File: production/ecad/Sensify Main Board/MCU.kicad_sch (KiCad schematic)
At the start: 0 parts

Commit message: step, mod, sym files for ESP32-WROOM-32, imported into schematic
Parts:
- added U1: ESP32-WROOM-32, ESP32-WROOM-32:MODULE_ESP32-WROOM-32, symbol ESP32-WROOM-32:ESP32-WROOM-32
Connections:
- new net: U1.1 (GND), U1.15 (GND), U1.38 (GND), U1.39_1 (GND), U1.39_10 (GND), U1.39_11 (GND), U1.39_12 (GND), U1.39_13 (GND), U1.39_14 (GND), U1.39_15 (GND), U1.39_16 (GND), U1.39_17 (GND), U1.39_18 (GND), U1.39_19 (GND), U1.39_2 (GND), U1.39_20 (GND), U1.39_21 (GND), U1.39_3 (GND), U1.39_4 (GND), U1.39_5 (GND), U1.39_6 (GND), U1.39_7 (GND), U1.39_8 (GND), U1.39_9 (GND)
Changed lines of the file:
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@@
 (kicad_sch (version 20230121) (generator eeschema)
   (paper "A4")
+  (symbol (lib_id "ESP32-WROOM-32:ESP32-WROOM-32") (at 151.13 100.33 0) (unit 1)
+    (in_bom yes) (on_board yes) (dnp no) (fields_autoplaced)
+    (property "Reference" "U1" (at 151.13 59.69 0)
+      (effects (font (size 1.27 1.27)))
+    )
+    (property "Value" "ESP32-WROOM-32" (at 151.13 62.23 0)
+      (effects (font (size 1.27 1.27)))
+    )
+    (property "Footprint" "ESP32-WROOM-32:MODULE_ESP32-WROOM-32" (at 151.13 100.33 0)
+      (effects (font (size 1.27 1.27)) (justify bottom) hide)
+    )
+    (property "Datasheet" "" (at 151.13 100.33 0)
+      (effects (font (size 1.27 1.27)) hide)
+    )
+    (property "MF" "Espressif Systems" (at 151.13 100.33 0)
+      (effects (font (size 1.27 1.27)) (justify bottom) hide)
+    )
+    (property "MAXIMUM_PACKAGE_HEIGHT" "3.2 mm" (at 151.13 100.33 0)
+      (effects (font (size 1.27 1.27)) (justify bottom) hide)
+    )
+    (property "Package" "None" (at 151.13 100.33 0)
+      (effects (font (size 1.27 1.27)) (justify bottom) hide)
+    )
+    (property "Price" "None" (at 151.13 100.33 0)
+      (effects (font (size 1.27 1.27)) (justify bottom) hide)
+    )
+    (property "Check_prices" "https://www.snapeda.com/parts/ESP32-WROOM-32/Espressif+Systems/view-part/?ref=eda" (at 151.13 100.33 0)
+      (effects (font (size 1.27 1.27)) (justify bottom) hide)
+    )
+    (property "STANDARD" "Manufacturer Recommendations" (at 151.13 100.33 0)
+      (effects (font (size 1.27 1.27)) (justify bottom) hide)
+    )
+    (property "PARTREV" "2.9" (at 151.13 100.33 0)
+      (effects (font (size 1.27 1.27)) (justify bottom) hide)
+    )
+    (property "SnapEDA_Link" "https://www.snapeda.com/parts/ESP32-WROOM-32/Espressif+Systems/view-part/?ref=snap" (at 151.13 100.33 0)
+      (effects (font (size 1.27 1.27)) (justify bottom) hide)
+    )
+    (property "MP" "ESP32-WROOM-32" (at 151.13 100.33 0)
+      (effects (font (size 1.27 1.27)) (justify bottom) hide)
+    )
+    (property "Description" "\nBluetooth, WiFi 802.11b/g/n, Bluetooth v4.2 +EDR, Class 1, 2 and 3 Transceiver Module 2.4GHz ~ 2.5GHz Antenna Not Included, U.FL Surface Mount\n" (at 151.13 100.33 0)
+      (effects (font (size 1.27 1.27)) (justify bottom) hide)
+    )
+    (property "Availability" "In Stock" (at 151.13 100.33 0)
+      (effects (font (size 1.27 1.27)) (justify bottom) hide)
+    )
+    (property "MANUFACTURER" "Espressif Systems" (at 151.13 100.33 0)
+      (effects (font (size 1.27 1.27)) (justify bottom) hide)
+    )
+    (pin "39_6")
+    (pin "6")
+    (pin "3")
+    (pin "39_5")
+    (pin "4")
+    (pin "39_13")
+    (pin "9")
+    (pin "25")
+    (pin "39_3")
+    (pin "34")
+    (pin "38")
+    (pin "24")
+    (pin "8")
+    (pin "22")
+    (pin "32")
+    (pin "39_11")
+    (pin "37")
+    (pin "39_15")
+    (pin "39_12")
+    (pin "21")
+    (pin "39_16")
+    (pin "27")
+    (pin "39_18")
+    (pin "39_19")
+    (pin "29")
+    (pin "33")
+    (pin "20")
+    (pin "39_14")
+    (pin "39_21")
+    (pin "39_4")
+    (pin "39_9")
+    (pin "39_10")
+    (pin "7")
+    (pin "5")
+    (pin "36")
+    (pin "39_2")
+    (pin "2")
+    (pin "31")
+    (pin "39_7")
+    (pin "30")
+    (pin "39_1")
+    (pin "39_8")
+    (pin "23")
+    (pin "26")
+    (pin "28")
+    (pin "39_17")
+    (pin "35")
+    (pin "39_20")
+    (pin "11")
+    (pin "15")
+    (pin "12")
+    (pin "16")
+    (pin "17")
+    (pin "18")
+    (pin "19")
+    (pin "13")
+    (pin "1")
+    (pin "14")
+    (pin "10")
+    (instances
+      (project "Sensify Main Board"
+        (path "/9a7ba7c3-7d28-4a83-bdbc-38fbff59fcbe/ec3ae12c-a69a-4cda-a73d-a33c865c767e"
+          (reference "U1") (unit 1)
+        )
+      )
+    )
+  )
 )

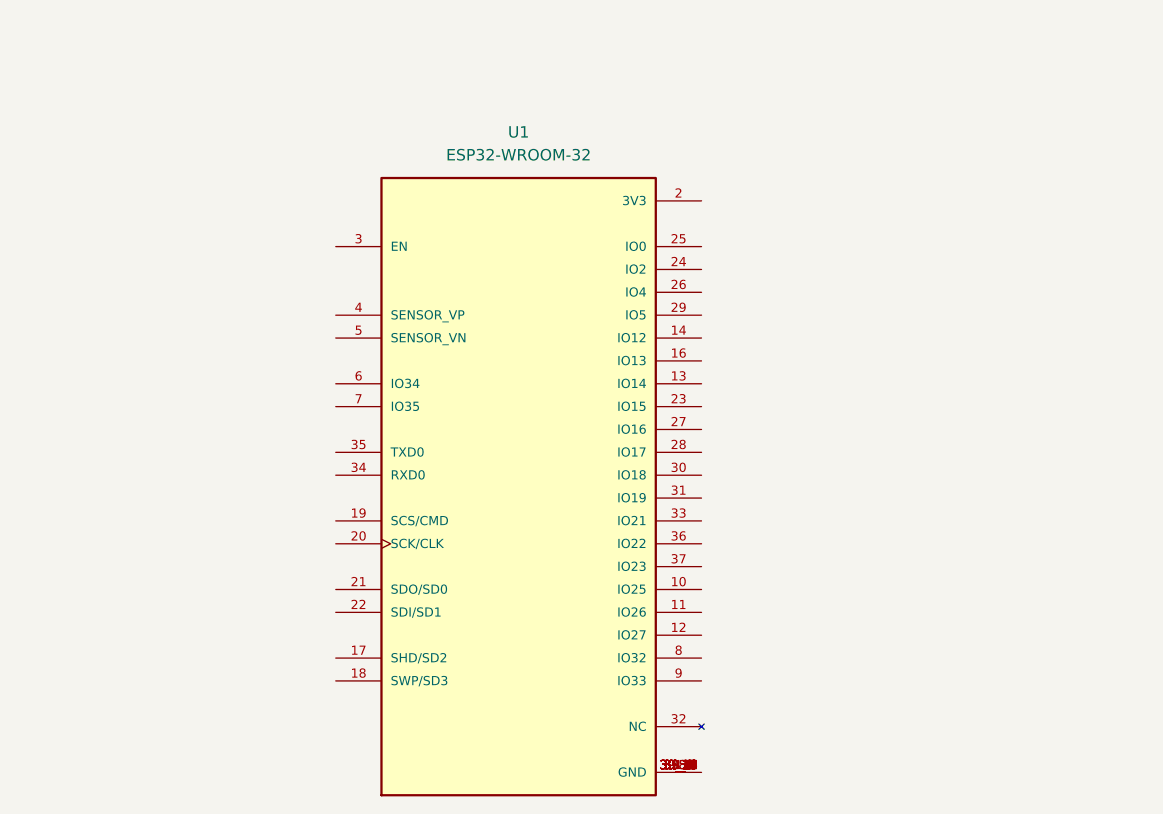
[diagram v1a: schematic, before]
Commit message: mostly done schematic i think. having trouble finding some parts
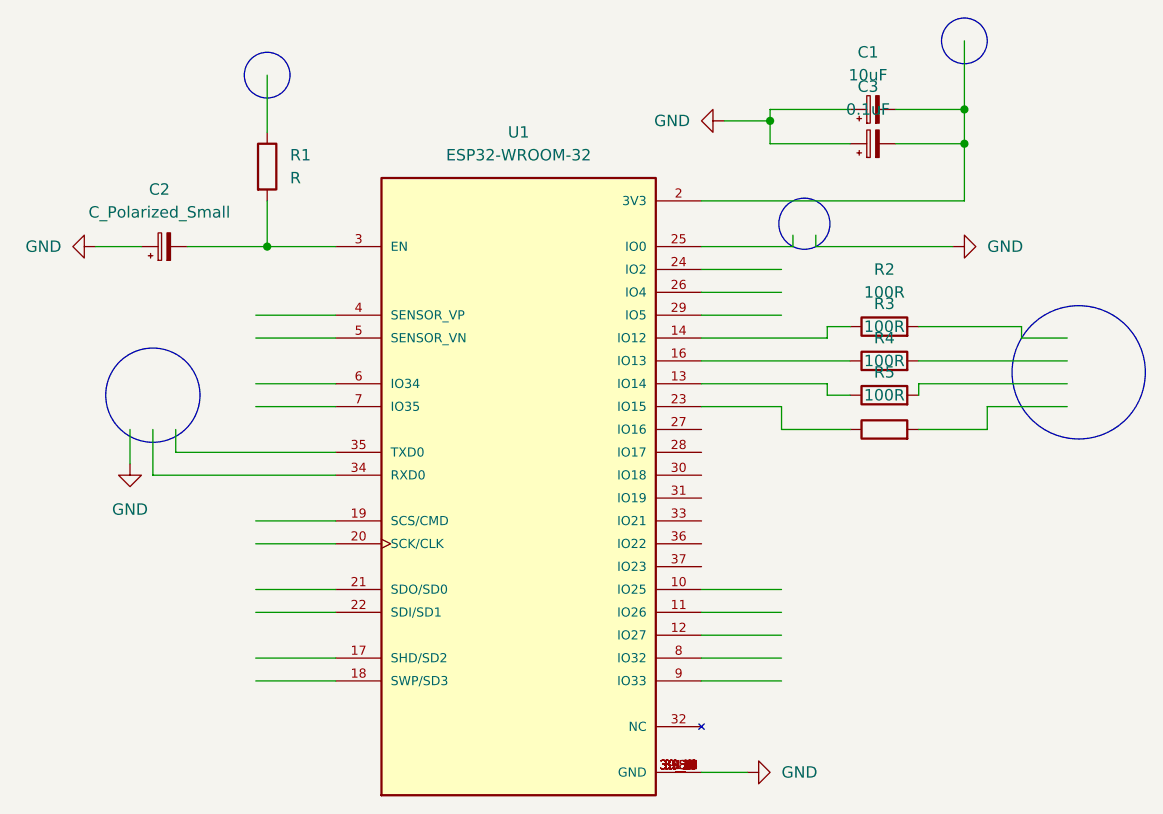
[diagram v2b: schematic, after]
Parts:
- added C1: 10uF, symbol Device:C_Polarized_Small
- added C2: C_Polarized_Small, symbol Device:C_Polarized_Small
- added C3: 0.1uF, symbol Device:C_Polarized_Small
- added R1: R, symbol Device:R
- added R2, R3, R4, R5: 100R, symbol Device:R
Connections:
- net GND: now reaches U1.1 (GND), U1.15 (GND), U1.38 (GND), U1.39_1 (GND), U1.39_10 (GND), U1.39_11 (GND), U1.39_12 (GND), U1.39_13 (GND), U1.39_14 (GND), U1.39_15 (GND), U1.39_16 (GND), U1.39_17 (GND), U1.39_18 (GND), U1.39_19 (GND), U1.39_2 (GND), U1.39_20 (GND), U1.39_21 (GND), U1.39_3 (GND), U1.39_4 (GND), U1.39_5 (GND), U1.39_6 (GND), U1.39_7 (GND), U1.39_8 (GND), U1.39_9 (GND)
- net GND: now also C1.1, C2.1, C3.1
- net at U1.13 (IO14): now also R4.1
- net at U1.14 (IO12): now also R2.1
- net at U1.16 (IO13): now also R3.1
- net at U1.2 (3V3): now also C1.2, C3.2
- net at U1.23 (IO15): now also R5.1
- net at U1.3 (EN): now also C2.2, R1.2

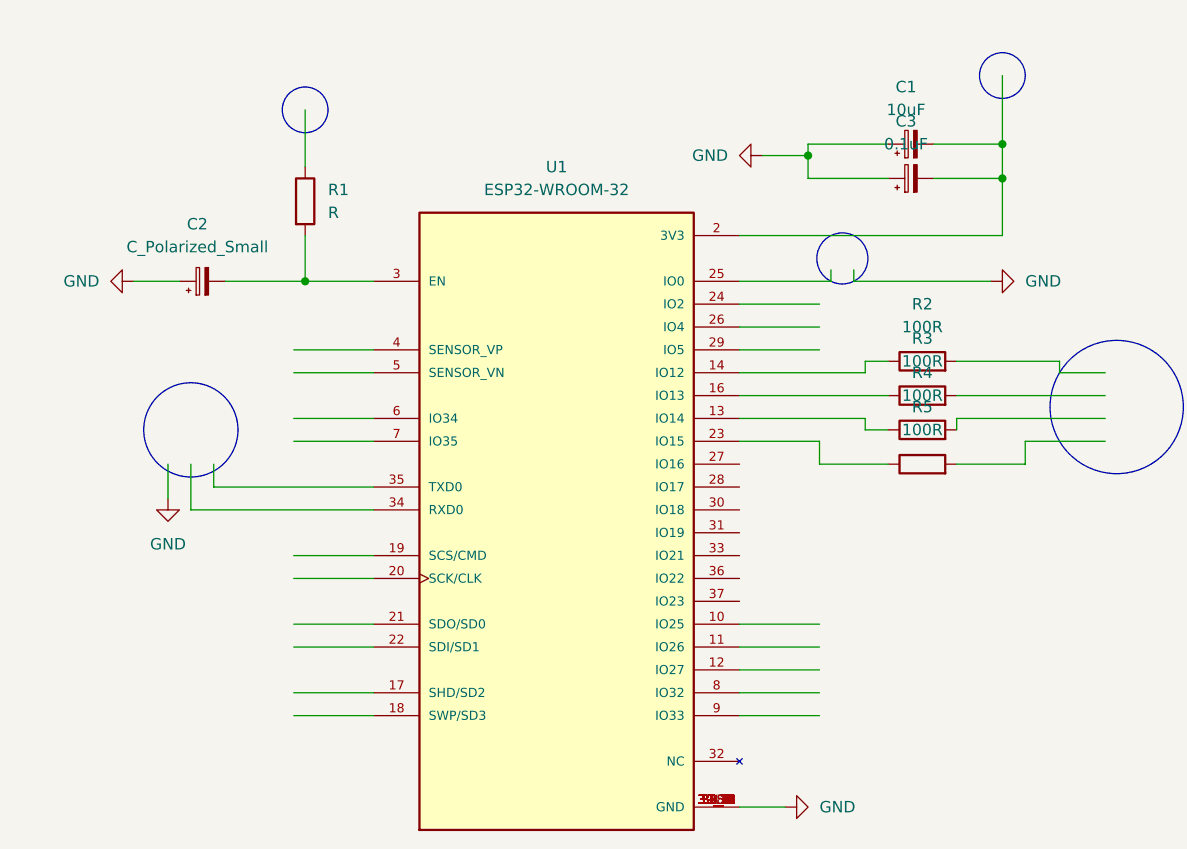
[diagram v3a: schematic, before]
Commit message: adding hierarchical labels
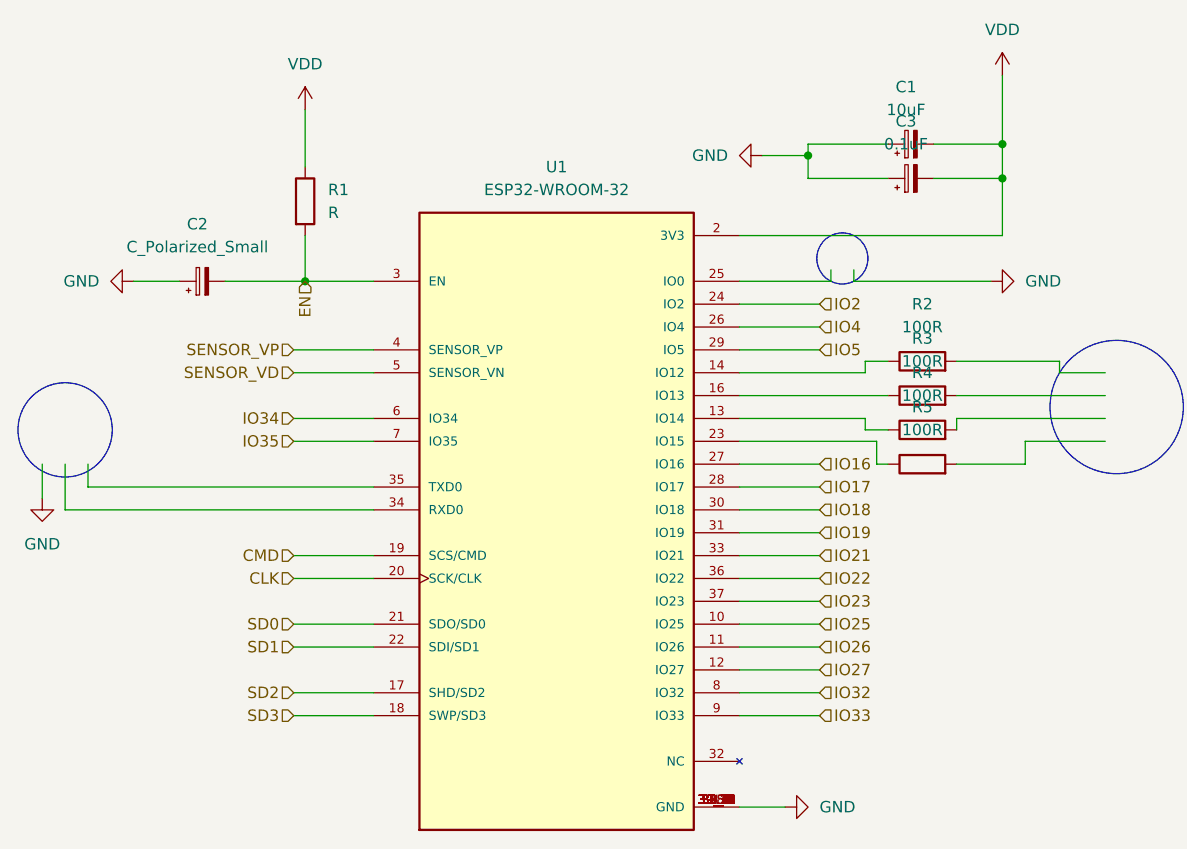
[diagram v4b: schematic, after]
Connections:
- net IO25: now reaches U1.10 (IO25)
- net IO26: now reaches U1.11 (IO26)
- net IO27: now reaches U1.12 (IO27)
- net SD2: now reaches U1.17 (SHD/SD2)
- net SD3: now reaches U1.18 (SWP/SD3)
- net CMD: now reaches U1.19 (SCS/CMD)
- net VDD: now reaches C1.2, C3.2, U1.2 (3V3)
- net VDD: now also R1.1
- net CLK: now reaches U1.20 (SCK/CLK)
- net SD0: now reaches U1.21 (SDO/SD0)
- net SD1: now reaches U1.22 (SDI/SD1)
- net IO2: now reaches U1.24 (IO2)
- net IO4: now reaches U1.26 (IO4)
- net IO16: now reaches U1.27 (IO16)
- net IO17: now reaches U1.28 (IO17)
- net IO5: now reaches U1.29 (IO5)
- net EN: now reaches C2.2, R1.2, U1.3 (EN)
- net IO18: now reaches U1.30 (IO18)
- net IO19: now reaches U1.31 (IO19)
- net IO21: now reaches U1.33 (IO21)
- net IO22: now reaches U1.36 (IO22)
- net IO23: now reaches U1.37 (IO23)
- net SENSOR_VP: now reaches U1.4 (SENSOR_VP)
- net SENSOR_VD: now reaches U1.5 (SENSOR_VN)
- net IO34: now reaches U1.6 (IO34)
- net IO35: now reaches U1.7 (IO35)
- net IO32: now reaches U1.8 (IO32)
- net IO33: now reaches U1.9 (IO33)

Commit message: schematic but V coming in clutch
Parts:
- added J1: MTDI, symbol Connector:Conn_01x01_Socket
- added J2: MTCK, symbol Connector:Conn_01x01_Socket
- added J3: MTMS, symbol Connector:Conn_01x01_Socket
- added J4: MTDO, symbol Connector:Conn_01x01_Socket
- added U2: TXB0104D, Package_SO:SOIC-14_3.9x8.7mm_P1.27mm, symbol Logic_LevelTranslator:TXB0104D
- added U4: CP2102N-Axx-xQFN28, Package_DFN_QFN:QFN-28-1EP_5x5mm_P0.5mm_EP3.35x3.35mm, symbol Interface_USB:CP2102N-Axx-xQFN28
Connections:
- net GND: now also U4.29 (GND), U4.3 (GND)
- net MTMS: now reaches R4.2
- net MTMS: now also J3.1 (Pin_1)
- net at U1.34 (RXD0): now also U4.25 (RXD)
- net at U1.35 (TXD0): now also U4.26 (TXD)
- net at R2.2: now also J1.1 (Pin_1)
- net MTCK: now reaches R3.2
- net MTCK: now also J2.1 (Pin_1)
- net MTDO: now reaches R5.2
- net MTDO: now also J4.1 (Pin_1)
- net IO21 renamed SDA
- net IO22 renamed SCL

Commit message: New MCU
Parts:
- added C12, C22, C23: 0.1uF, symbol Device:C
- added C13: 10uF, symbol Device:C
- added C20: 4.7uF, symbol Device:C
- added C21: 100nF, symbol Device:C
- added J5: 1332645, 1332645:PHOENIX_1332645, symbol USBC CONN:1332645
- added R12, R26, R31, R32: 10k, symbol Device:R
- added R20: 22.1k, symbol Device:R
- added R21: 47.5k, symbol Device:R
- added R27, R28: 0, symbol Device:R
- added R29, R30: 5.1k, symbol Device:R
- added R33, R34: 1k, symbol Device:R
- added SW2, SW3: SW_Push, symbol Switch:SW_Push
- added U10, U9: AO3400A, SOT-23-3L_AOS, symbol A03400A:AO3400A
- added U7: ESP32-WROOM-32UE_M113EH6400UH3Q0_, ESP32-WROOM-32UE_M113EH6400UH3Q0_:MODULE_ESP32-WROOM-32UE_M113EH6400UH3Q0_, symbol EP32UE:ESP32-WROOM-32UE_M113EH6400UH3Q0_
- added U8: CP2102N-A01-GQFN28, QFN28_5X5_SIL, symbol CP210:CP2102N-A01-GQFN28
- R1: footprint (none) -> Resistor_SMD:R_0805_2012Metric
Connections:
- net EN: now also C22.1, R33.2, SW2.1, U7.3 (EN), U9.3 (D)
- net GND: now also C12.2, C13.2, C20.2, C21.2, C22.2, C23.2, J5.A1_B12 (GND_A), J5.B1_A12 (GND_B), J5.SH1 (SHIELD), J5.SH2 (SHIELD__1), J5.SH3 (SHIELD__2), J5.SH4 (SHIELD__3), R21.2, R26.2, R29.2, R30.2, SW2.2, SW3.2, U7.1 (GND), U7.15 (GND), U7.38 (GND), U7.39_1 (GND), U7.39_10 (GND), U7.39_11 (GND), U7.39_12 (GND), U7.39_13 (GND), U7.39_14 (GND), U7.39_15 (GND), U7.39_16 (GND), U7.39_17 (GND), U7.39_18 (GND), U7.39_19 (GND), U7.39_2 (GND), U7.39_20 (GND), U7.39_21 (GND), U7.39_3 (GND), U7.39_4 (GND), U7.39_5 (GND), U7.39_6 (GND), U7.39_7 (GND), U7.39_8 (GND), U7.39_9 (GND), U8.29 (EPAD), U8.3 (GND)
- net SCL: now also U7.36 (IO22)
- net SDA: now also U7.33 (IO21)
- net SENSOR_VD: no longer names the net of U1.5 (SENSOR_VN)
- net SENSOR_VP: no longer names the net of U1.4 (SENSOR_VP)
- new net: R26.1, U8.11 (SUSPENDb)
- new net: J5.B5 (CC2), R29.1
- new net: R32.2, U10.1 (G)
- new net: R12.2, U8.9 (RSTb)
- new net: R31.2, U9.1 (G)
- new net: R20.2, R21.1, U8.8 (VBUS)
- new net: R28.1, U8.25 (RXD)
- new net: R27.1, U8.26 (TXD)
- new net: J5.A5 (CC1), R30.1
- new net: U7.17 (NC), U7.18 (NC), U7.19 (NC), U7.20 (NC), U7.21 (NC), U7.22 (NC)
- new net +3V3: C12.1, C13.1, C20.1, C21.1, R12.1, R33.1, R34.1, U7.2 (3V3), U8.6 (VDD), U8.7 (VREGIN)
- new net DTR: R31.1, U10.2 (S), U8.28 (DTR)
- new net INTERRUPT2_IMU: U7.9 (IO33)
- new net IO0: C23.1, R34.2, SW3.1, U10.3 (D), U7.25 (IO0)
- new net MCU_WAKEUP: U7.8 (IO32)
- new net RTS: R32.1, U8.24 (RTS), U9.2 (S)
- new net UART_RXD: R28.2, U7.35 (TXD0)
- new net UART_TXD: R27.2, U7.34 (RXD0)
- new net USB_D+: J5.A6 (DP1), J5.B6 (DP2), U8.4 (D+)
- new net USB_D-: J5.A7 (DN1), J5.B7 (DN2), U8.5 (D-)
- new net VBUS: J5.A4_B9 (VBUS_A), J5.B4_A9 (VBUS_B), R20.1
- no-connect marks 0 -> 24
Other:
- note added: "Charlie Current Schematic"
- note added: "ESP32 WROOM UE"
- note added: "Reset Button for MCU"
- note added: "USB to UART"
- note added: "USBC Connector"
- note added: "Vas Current Schematic"
- moved on the sheet: C1, C2, C3, J1, J2, J3, J4, R1, R2, R3, R4, R5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

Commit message: Finalized MCU
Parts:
- removed C1: 10uF, symbol Device:C_Polarized_Small
- removed C2: C_Polarized_Small, symbol Device:C_Polarized_Small
- removed C3: 0.1uF, symbol Device:C_Polarized_Small
- removed J1: MTDI, symbol Connector:Conn_01x01_Socket
- removed J2: MTCK, symbol Connector:Conn_01x01_Socket
- removed J3: MTMS, symbol Connector:Conn_01x01_Socket
- removed J4: MTDO, symbol Connector:Conn_01x01_Socket
- removed R1: R, Resistor_SMD:R_0805_2012Metric, symbol Device:R
- removed R2, R3, R4, R5: 100R, symbol Device:R
- removed U1: ESP32-WROOM-32, ESP32-WROOM-32:MODULE_ESP32-WROOM-32, symbol ESP32-WROOM-32:ESP32-WROOM-32
- removed U2: TXB0104D, Package_SO:SOIC-14_3.9x8.7mm_P1.27mm, symbol Logic_LevelTranslator:TXB0104D
- removed U4: CP2102N-Axx-xQFN28, Package_DFN_QFN:QFN-28-1EP_5x5mm_P0.5mm_EP3.35x3.35mm, symbol Interface_USB:CP2102N-Axx-xQFN28
- removed U7: ESP32-WROOM-32UE_M113EH6400UH3Q0_, ESP32-WROOM-32UE_M113EH6400UH3Q0_:MODULE_ESP32-WROOM-32UE_M113EH6400UH3Q0_, symbol EP32UE:ESP32-WROOM-32UE_M113EH6400UH3Q0_
- added J6, J7: Conn_01x06_Socket, symbol Connector:Conn_01x06_Socket
- added U11: ESP32-WROOM-32E__16MB_, ESP32-WROOM-32E__16MB_:XCVR_ESP32-WROOM-32E__16MB_, symbol ESP32-WROOM-32E:ESP32-WROOM-32E__16MB_
- C12, C13, C20, C21, C22, C23: footprint (none) -> Capacitor_SMD:C_0402_1005Metric
- R12, R20, R21, R26, R27, R28, R29, R30, R31, R32, R33, R34: footprint (none) -> Resistor_SMD:R_0402_1005Metric
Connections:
- net +3V3: now also J7.6 (Pin_6), U11.2 (3V3)
- net EN: now also U11.3 (EN)
- net GND: now also J7.4 (Pin_4), U11.1 (GND), U11.15 (GND), U11.38 (GND), U11.39_1 (GND), U11.39_2 (GND), U11.39_3 (GND), U11.39_4 (GND), U11.39_5 (GND), U11.39_6 (GND), U11.39_7 (GND), U11.39_8 (GND), U11.39_9 (GND)
- net INTERRUPT2_IMU: now also U11.9 (IO33)
- net IO0: now also U11.25 (IO0)
- net MCU_WAKEUP: now also U11.8 (IO32)
- net SCL: now also U11.10 (IO25)
- net SDA: now also U11.37 (IO23)
- net UART_RXD: now also U11.35 (TXD0)
- net UART_TXD: now also U11.34 (RXD0)
- new net: J6.2 (Pin_2), U11.29 (IO5)
- new net: J6.3 (Pin_3), U11.14 (IO12)
- new net: J6.4 (Pin_4), U11.16 (IO13)
- new net: J6.5 (Pin_5), U11.13 (IO14)
- new net: J6.6 (Pin_6), U11.23 (IO15)
- new net: U11.17 (NC), U11.18 (NC), U11.19 (NC), U11.20 (NC), U11.21 (NC), U11.22 (NC)
- new net: J7.1 (Pin_1), U11.27 (IO16)
- new net: J7.2 (Pin_2), U11.28 (IO17)
- new net: J7.3 (Pin_3), U11.30 (IO18)
- new net: J7.5 (Pin_5), U11.33 (IO21)
- new net +5V: J6.1 (Pin_1)
- no-connect marks 24 -> 30
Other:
- note added: "ESP32 WROOM 32E"
- note removed: "Charlie Current Schematic"
- note removed: "ESP32 WROOM UE"
- note removed: "Vas Current Schematic"
- moved on the sheet: C12, C13, J5, R29, R30
